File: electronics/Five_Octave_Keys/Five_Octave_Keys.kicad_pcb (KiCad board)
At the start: 2 copper layers, 285.8 x 95.2 mm, 126 parts, among them J1 FFC Connector, SW1 Key Esc, SW10 Key 9, SW11 Key 0, SW12 Key -, SW13 Key =, SW14 Key \, SW15 Key `, SW16 Key Tab, SW17 Key Q, SW18 Key W, SW19 Key E, SW2 Key 1, SW20 Key R, SW21 Key T, SW22 Key Y, SW23 Key U, SW24 Key I, SW25 Key O, SW26 Key P, SW27 Key [, SW28 Key ], SW29 Key BS, SW3 Key 2, SW30 Key Caps, SW31 Key A, SW32 Key S, SW33 Key D, SW34 Key F, SW35 Key G, SW36 Key H, SW37 Key J, SW38 Key K, SW39 Key L, SW4 Key 3, SW40 Key ;, SW41 Key ', SW42 Key Return, SW43 Key Shift, SW44 Key Z, SW45 Key X, SW46 Key C, SW47 Key V, SW48 Key B, SW49 Key N, SW5 Key 4, SW50 Key M, SW51 Key ,, SW52 Key ., SW53 Key /, SW54 Key Shift, SW55 Key Fn, SW56 Key Ctrl, SW57 Key Opt, SW58 Key Cmd, SW59 Key Space, SW6 Key 5, SW60 Key Cmd, SW61 Key MO(1), SW7 Key 6, SW8 Key 7, SW9 Key 8

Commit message: Wire diodes to switches
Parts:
- moved J1 52.4 mm to (152.4, 114.3)
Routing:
- net Net-(D17-A): track 0.00 -> 5.41 mm
- net Net-(D16-A): track 0.00 -> 5.41 mm
- net Net-(D60-A): track 0.00 -> 5.41 mm
- net Net-(D46-A): track 0.00 -> 5.41 mm
- net Net-(D21-A): track 0.00 -> 5.41 mm
- net Net-(D57-A): track 0.00 -> 5.41 mm
- net Net-(D56-A): track 0.00 -> 5.41 mm
- net Net-(D9-A): track 0.00 -> 5.41 mm
- net Net-(D4-A): track 0.00 -> 5.41 mm
- net Net-(D61-A): track 0.00 -> 5.41 mm
- net Net-(D53-A): track 0.00 -> 5.41 mm
- net Net-(D36-A): track 0.00 -> 5.41 mm
- net Net-(D11-A): track 0.00 -> 5.41 mm
- net Net-(D49-A): track 0.00 -> 5.41 mm
- net Net-(D47-A): track 0.00 -> 5.41 mm
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
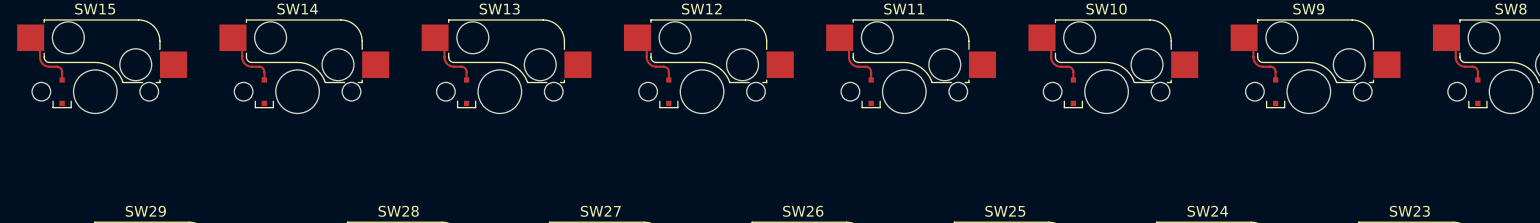
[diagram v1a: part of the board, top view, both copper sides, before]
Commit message: Route some diodes
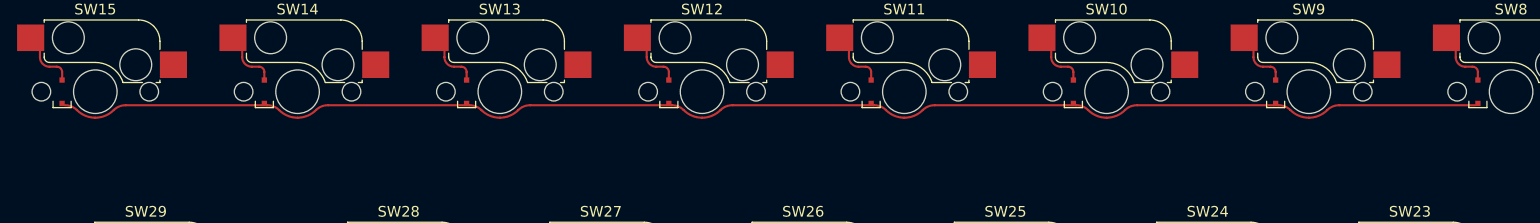
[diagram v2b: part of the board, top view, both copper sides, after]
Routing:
- net ROW4: track 0.00 -> 137.0 mm
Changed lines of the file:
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@@
   (title_block
     (title "Five Octave - Keys")
-    (date "2023-07-31")
-    (rev "0.1.1")
+    (date "2023-08-01")
+    (rev "0.1.2")
     (comment 1 "https://github.com/takayoshiotake/five-octave-61-key-keyboard")
   )
@@
     )
   )
-  (footprint "Project_Library:D_SOD-323F" locked (layer "F.Cu")
+  (footprint "Project_Library:D_SOD-323F" (layer "F.Cu")
     (at 54.0225 38.1 90)
     (descr "SOD-323F")
@@
     (fp_line (start 0.9 0.7) (end -0.9 0.7)
       (stroke (width 0.1) (type solid)) (layer "F.Fab"))
-    (pad "1" smd rect locked (at -1.1 0 90) (size 0.5 0.5) (layers "F.Cu" "F.Paste" "F.Mask")
+    (pad "1" smd rect (at -1.1 0 90) (size 0.5 0.5) (layers "F.Cu" "F.Paste" "F.Mask")
       (net 9 "ROW4") (pinfunction "K") (pintype "passive"))
-    (pad "2" smd rect locked (at 1.1 0 90) (size 0.5 0.5) (layers "F.Cu" "F.Paste" "F.Mask")
+    (pad "2" smd rect (at 1.1 0 90) (size 0.5 0.5) (layers "F.Cu" "F.Paste" "F.Mask")
       (net 16 "Net-(D14-A)") (pinfunction "A") (pintype "passive"))
     (model "${KICAD6_3DMODEL_DIR}/Diode_SMD.3dshapes/D_SOD-323.wrl"
@@
     )
   )
-  (footprint "Project_Library:D_SOD-323F" locked (layer "F.Cu")
+  (footprint "Project_Library:D_SOD-323F" (layer "F.Cu")
     (at 34.9725 38.1 90)
     (descr "SOD-323F")
@@
     (fp_line (start 0.9 0.7) (end -0.9 0.7)
       (stroke (width 0.1) (type solid)) (layer "F.Fab"))
-    (pad "1" smd rect locked (at -1.1 0 90) (size 0.5 0.5) (layers "F.Cu" "F.Paste" "F.Mask")
+    (pad "1" smd rect (at -1.1 0 90) (size 0.5 0.5) (layers "F.Cu" "F.Paste" "F.Mask")
       (net 9 "ROW4") (pinfunction "K") (pintype "passive"))
-    (pad "2" smd rect locked (at 1.1 0 90) (size 0.5 0.5) (layers "F.Cu" "F.Paste" "F.Mask")
+    (pad "2" smd rect (at 1.1 0 90) (size 0.5 0.5) (layers "F.Cu" "F.Paste" "F.Mask")
       (net 17 "Net-(D15-A)") (pinfunction "A") (pintype "passive"))
     (model "${KICAD6_3DMODEL_DIR}/Diode_SMD.3dshapes/D_SOD-323.wrl"
@@
   (arc (start 186.8725 35.745) (mid 187.226053 35.891447) (end 187.3725 36.245) (width 0.2) (layer "F.Cu") (net 8))
   (arc (start 185.285 34.845) (mid 185.548604 35.481396) (end 186.185 35.745) (width 0.2) (layer "F.Cu") (net 8))
+  (segment (start 98.1275 39.375) (end 111.4225 39.375) (width 0.2) (layer "F.Cu") (net 9))
+  (segment (start 136.2275 39.375) (end 149.5225 39.375) (width 0.2) (layer "F.Cu") (net 9))
+  (segment (start 155.2775 39.375) (end 168.0725 39.375) (width 0.2) (layer "F.Cu") (net 9))
+  (segment (start 40.9775 39.375) (end 54.2725 39.375) (width 0.2) (layer "F.Cu") (net 9))
+  (segment (start 79.0775 39.375) (end 92.3725 39.375) (width 0.2) (layer "F.Cu") (net 9))
+  (segment (start 117.1775 39.375) (end 130.4725 39.375) (width 0.2) (layer "F.Cu") (net 9))
+  (segment (start 60.0275 39.375) (end 73.3225 39.375) (width 0.2) (layer "F.Cu") (net 9))
+  (arc (start 98.1275 39.375) (mid 97.489065 39.493877) (end 96.982412 39.832412) (width 0.2) (layer "F.Cu") (net 9))
+  (arc (start 54.2725 39.375) (mid 54.910935 39.493877) (end 55.417588 39.832412) (width 0.2) (layer "F.Cu") (net 9))
+  (arc (start 116.032412 39.832412) (mid 115.237575 40.363505) (end 114.3 40.55) (width 0.2) (layer "F.Cu") (net 9))
+  (arc (start 117.1775 39.375) (mid 116.539065 39.493877) (end 116.032412 39.832412) (width 0.2) (layer "F.Cu") (net 9))
+  (arc (start 155.2775 39.375) (mid 154.639065 39.493877) (end 154.132412 39.832412) (width 0.2) (layer "F.Cu") (net 9))
+  (arc (start 96.982412 39.832412) (mid 96.187575 40.363505) (end 95.25 40.55) (width 0.2) (layer "F.Cu") (net 9))
+  (arc (start 93.517588 39.832412) (mid 94.312425 40.363505) (end 95.25 40.55) (width 0.2) (layer "F.Cu") (net 9))
+  (arc (start 150.667588 39.832412) (mid 151.462425 40.363505) (end 152.4 40.55) (width 0.2) (layer "F.Cu") (net 9))
+  (arc (start 55.417588 39.832412) (mid 56.212425 40.363505) (end 57.15 40.55) (width 0.2) (layer "F.Cu") (net 9))
+  (arc (start 36.367588 39.832412) (mid 37.162425 40.363505) (end 38.1 40.55) (width 0.2) (layer "F.Cu") (net 9))
+  (arc (start 35.2225 39.375) (mid 35.860935 39.493877) (end 36.367588 39.832412) (width 0.2) (layer "F.Cu") (net 9))
+  (arc (start 79.0775 39.375) (mid 78.439065 39.493877) (end 77.932412 39.832412) (width 0.2) (layer "F.Cu") (net 9))
+  (arc (start 39.832412 39.832412) (mid 39.037575 40.363505) (end 38.1 40.55) (width 0.2) (layer "F.Cu") (net 9))
+  (arc (start 130.4725 39.375) (mid 131.110935 39.493877) (end 131.617588 39.832412) (width 0.2) (layer "F.Cu") (net 9))
+  (arc (start 73.3225 39.375) (mid 73.960935 39.493877) (end 74.467588 39.832412) (width 0.2) (layer "F.Cu") (net 9))
+  (arc (start 154.132412 39.832412) (mid 153.337575 40.363505) (end 152.4 40.55) (width 0.2) (layer "F.Cu") (net 9))
+  (arc (start 92.3725 39.375) (mid 93.010935 39.493877) (end 93.517588 39.832412) (width 0.2) (layer "F.Cu") (net 9))
+  (arc (start 111.4225 39.375) (mid 112.060935 39.493877) (end 112.567588 39.832412) (width 0.2) (layer "F.Cu") (net 9))
+  (arc (start 135.082412 39.832412) (mid 134.287575 40.363505) (end 133.35 40.55) (width 0.2) (layer "F.Cu") (net 9))
+  (arc (start 40.9775 39.375) (mid 40.339065 39.493877) (end 39.832412 39.832412) (width 0.2) (layer "F.Cu") (net 9))
+  (arc (start 60.0275 39.375) (mid 59.389065 39.493877) (end 58.882412 39.832412) (width 0.2) (layer "F.Cu") (net 9))
+  (arc (start 112.567588 39.832412) (mid 113.362425 40.363505) (end 114.3 40.55) (width 0.2) (layer "F.Cu") (net 9))
+  (arc (start 131.617588 39.832412) (mid 132.412425 40.363505) (end 133.35 40.55) (width 0.2) (layer "F.Cu") (net 9))
+  (arc (start 136.2275 39.375) (mid 135.589065 39.493877) (end 135.082412 39.832412) (width 0.2) (layer "F.Cu") (net 9))
+  (arc (start 149.5225 39.375) (mid 150.160935 39.493877) (end 150.667588 39.832412) (width 0.2) (layer "F.Cu") (net 9))
+  (arc (start 74.467588 39.832412) (mid 75.262425 40.363505) (end 76.2 40.55) (width 0.2) (layer "F.Cu") (net 9))
+  (arc (start 77.932412 39.832412) (mid 77.137575 40.363505) (end 76.2 40.55) (width 0.2) (layer "F.Cu") (net 9))
+  (arc (start 58.882412 39.832412) (mid 58.087575 40.363505) (end 57.15 40.55) (width 0.2) (layer "F.Cu") (net 9))
   (segment (start 168.3225 36.245) (end 168.3225 37) (width 0.2) (layer "F.Cu") (net 10))
   (segment (start 166.235 33.02) (end 166.235 34.845) (width 0.2) (layer "F.Cu") (net 10))
@@
     )
   )
-  (group "" (id aba71723-b7cc-49a4-bfdb-4c151b2d6ff3)
-    (members
-      4a665656-f55c-494f-84f7-51ded52ba664
-      6cb4f516-879e-423c-adc4-76c2cc338d06
-      a2a86880-fc0c-48d3-971b-a920675ffe21
-      c53227f6-1cbc-44a4-aaf4-85c6a9434b57
-      ebd25395-0218-4633-9fe0-677948a8d479
-    )
-  )

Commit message: Adjust key-matrix
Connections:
- SW33 pad 2: COL4 -> COL5
- SW45 pad 2: COL5 -> COL4
- SW46 pad 2: COL5 -> COL4
- SW47 pad 2: COL6 -> COL5
- SW48 pad 2: COL7 -> COL6
- SW59 pad 2: COL5 -> COL7
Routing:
- net ROW3: track 0.00 -> 186.8 mm
- net ROW6: track 0.00 -> 160.5 mm
- net ROW2: track 0.00 -> 148.2 mm
- net ROW5: track 0.00 -> 141.7 mm
- net ROW7: track 0.00 -> 140.0 mm
- net ROW0: track 0.00 -> 116.8 mm
- net ROW1: track 0.00 -> 102.4 mm

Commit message: Adjust key-matrix
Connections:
- SW32 pad 2: COL3 -> COL4
- SW45 pad 2: COL4 -> COL3
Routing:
- net COL0: track 0.00 -> 143.6 mm, vias 0 -> 2
- net COL3: track 0.00 -> 104.6 mm, vias 0 -> 8
- net COL5: track 0.00 -> 104.6 mm, vias 0 -> 8
- net COL4: track 0.00 -> 104.6 mm, vias 0 -> 8
- net COL2: track 0.00 -> 104.6 mm, vias 0 -> 8
- net COL1: track 0.00 -> 81.8 mm, vias 0 -> 8
- net COL6: track 0.00 -> 65.7 mm, vias 0 -> 6
- net COL7: track 0.00 -> 22.5 mm, vias 0 -> 2
- net ROW5: track 141.7 -> 143.0 mm

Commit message: Adjust key-matrix
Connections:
- SW17 pad 2: COL2 -> COL3
- SW18 pad 2: COL3 -> COL4
- SW19 pad 2: COL4 -> COL5
- SW2 pad 2: COL1 -> COL2
- SW20 pad 2: COL5 -> COL6
- SW21 pad 2: COL6 -> COL7
- SW3 pad 2: COL2 -> COL3
- SW31 pad 2: COL1 -> COL3
- SW4 pad 2: COL3 -> COL4
- SW44 pad 2: COL2 -> COL1
- SW45 pad 2: COL3 -> COL2
- SW46 pad 2: COL4 -> COL5
- SW47 pad 2: COL5 -> COL6
- SW48 pad 2: COL6 -> COL7
- SW5 pad 2: COL4 -> COL5
- SW59 pad 2: COL7 -> COL4
- SW6 pad 2: COL5 -> COL6
- SW7 pad 2: COL6 -> COL7
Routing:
- net COL7: track 22.5 -> 49.7 mm, vias 2 -> 4
- net COL2: track 104.6 -> 81.8 mm
- net COL1: track 81.8 -> 77.4 mm, vias 8 -> 6

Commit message: Update pcb
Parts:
- SW16: value Key Tab -> locked
- SW18: value Key W -> locked
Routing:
- net COL2: track 81.8 -> 409.5 mm, vias 8 -> 18
- net COL1: track 77.4 -> 325.5 mm, vias 6 -> 10
- net COL0: track 143.6 -> 383.3 mm
- net COL7: track 49.7 -> 275.3 mm, vias 4 -> 14
- net COL6: track 65.7 -> 277.7 mm, vias 6 -> 12
- net COL3: track 104.6 -> 265.0 mm, vias 8 -> 20
- net COL5: track 104.6 -> 252.2 mm, vias 8 -> 14
- net COL4: track 104.6 -> 204.8 mm, vias 8 -> 12
- net ROW2: track 148.2 -> 124.0 mm
- net ROW7: track 140.0 -> 116.8 mm
- net ROW3: track 186.8 -> 167.4 mm
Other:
- outline, holes or cut-outs redrawn

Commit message: Update Five_Octave_Keys.kicad_pcb
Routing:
- net COL4: track 204.8 -> 360.3 mm, vias 12 -> 18
- net COL3: track 265.0 -> 378.2 mm
- net COL5: track 252.2 -> 361.0 mm, vias 14 -> 16
- net COL6: track 277.7 -> 370.8 mm, vias 12 -> 16
- net COL7: track 275.3 -> 354.7 mm, vias 14 -> 18
- net ROW3: track 167.4 -> 117.4 mm

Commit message: Update Five_Octave_Keys.kicad_pcb
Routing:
- net ROW3: track 117.4 -> 230.4 mm, vias 0 -> 7
- net ROW0: track 116.8 -> 229.1 mm, vias 0 -> 2
- net ROW2: track 124.0 -> 226.0 mm, vias 0 -> 4
- net ROW4: track 137.0 -> 232.7 mm, vias 0 -> 2
- net ROW1: track 102.4 -> 198.2 mm, vias 0 -> 2
- net ROW5: track 143.0 -> 222.2 mm, vias 0 -> 2
- net ROW6: track 160.4 -> 216.6 mm, vias 0 -> 2
- net ROW7: track 116.8 -> 151.7 mm, vias 0 -> 2
- net COL7: track 354.7 -> 353.7 mm
- net COL6: track 370.8 -> 369.8 mm
- net COL0: track 383.3 -> 382.8 mm, vias 2 -> 6
